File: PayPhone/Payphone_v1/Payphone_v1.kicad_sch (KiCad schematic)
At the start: 70 parts, among them J1 JST_05, J10 PINHD_1x2_Male, J2 Molex_26-60-4030, J3 Molex_26-60-4040, J6 PINHD_1x5_Male, J7 PINHD_1x2_Male, J8 PINHD_1x2_Male, J9 PINHD_1x2_Male, K1 G6S-2, Q2 2N7000, Q3 IRF630, Q4 2N7000, Q5 2N7000, U1 MCP23008-xP, U2 MC34063AP, U3 UC3843AN

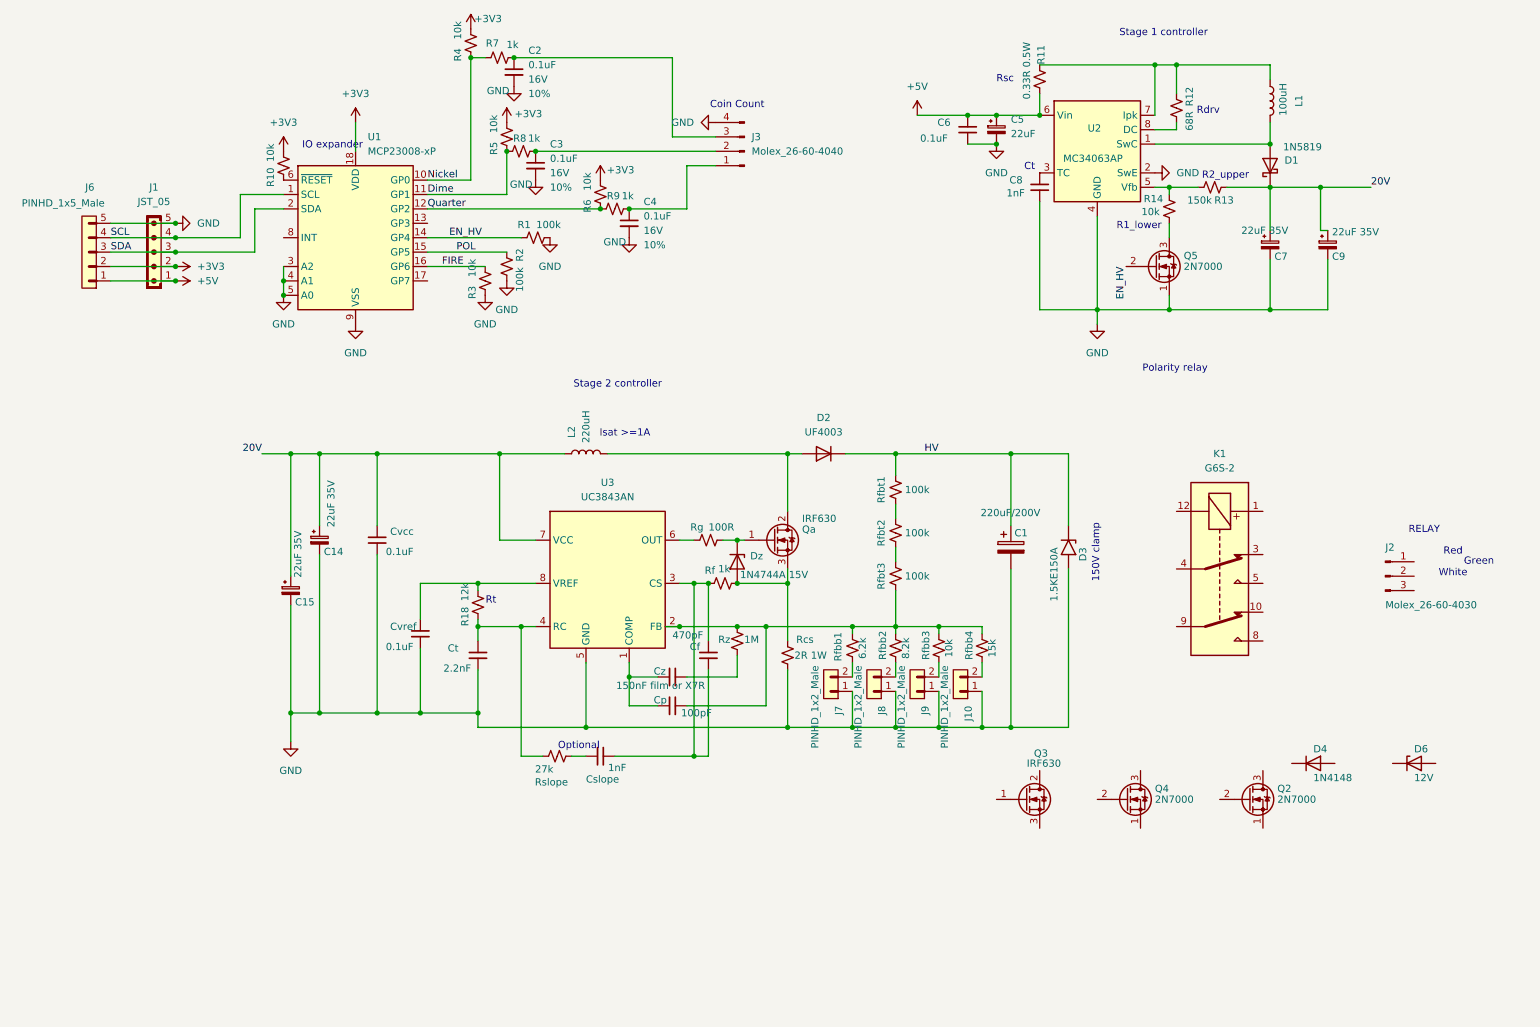
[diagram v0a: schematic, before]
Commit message: Payphone_v1: output stage connected by net labels (K1 contacts, COIL_A/B, RETURN, relay driver, Q4/Q6 gate drive, ISENSE), Q6 2N3906, R20-R26, C16 decoupling for U1; HV-class labels on SW2 and the HV resistor chains
Co-Authored-By: Claude Opus 5.5 <noreply@anthropic.com>
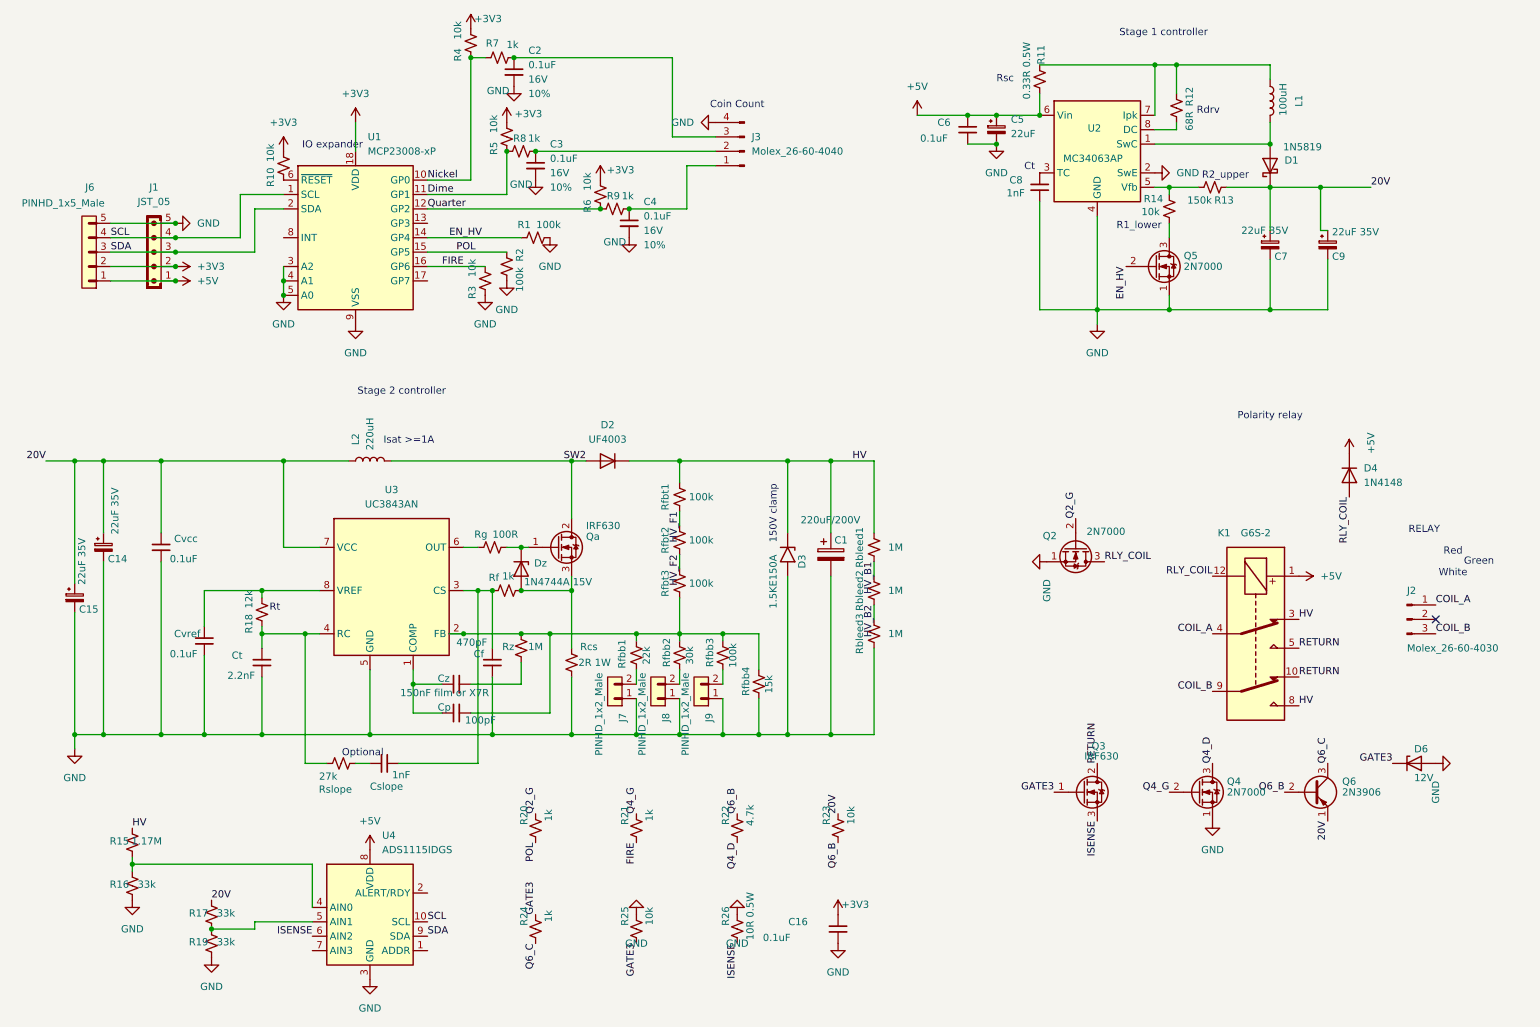
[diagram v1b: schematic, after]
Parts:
- removed J10: PINHD_1x2_Male, Connector_PinHeader_2.54mm:PinHeader_1x02_P2.54mm_Vertical, symbol PCM_SL_Pin_Headers:PINHD_1x2_Male
- added C16: 0.1uF, Capacitor_THT:C_Disc_D5.0mm_W2.5mm_P5.00mm, symbol Device:C_Small
- added Q6: 2N3906, Package_TO_SOT_THT:TO-92_Inline, symbol Transistor_BJT:2N3906
- added R15: 1.17M, Resistor_THT:R_Axial_DIN0207_L6.3mm_D2.5mm_P10.16mm_Horizontal, symbol PCM_SparkFun-Resistor:R_Small
- added R16, R17, R19: 33k, Resistor_THT:R_Axial_DIN0207_L6.3mm_D2.5mm_P10.16mm_Horizontal, symbol PCM_SparkFun-Resistor:R_Small
- added R20, R21, R24: 1k, Resistor_THT:R_Axial_DIN0207_L6.3mm_D2.5mm_P10.16mm_Horizontal, symbol PCM_SparkFun-Resistor:R_Small
- added R22: 4.7k, Resistor_THT:R_Axial_DIN0207_L6.3mm_D2.5mm_P10.16mm_Horizontal, symbol PCM_SparkFun-Resistor:R_Small
- added R23, R25: 10k, Resistor_THT:R_Axial_DIN0207_L6.3mm_D2.5mm_P10.16mm_Horizontal, symbol PCM_SparkFun-Resistor:R_Small
- added R26: 10R 0.5W, Resistor_THT:R_Axial_DIN0309_L9.0mm_D3.2mm_P12.70mm_Horizontal, symbol PCM_SparkFun-Resistor:R_Small
- added Rbleed1, Rbleed2, Rbleed3: 1M, Resistor_THT:R_Axial_DIN0207_L6.3mm_D2.5mm_P10.16mm_Horizontal, symbol PCM_SparkFun-Resistor:R_Small
- added U4: ADS1115IDGS, Package_SO:TSSOP-10_3x3mm_P0.5mm, symbol Analog_ADC:ADS1115IDGS
- Rfbb1: value 6.2k -> 22k
- Rfbb2: value 8.2k -> 30k
- Rfbb3: value 10k -> 100k
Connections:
- net +3V3: now also C16.1
- net +5V: now also D4.1 (K), K1.1, U4.8 (VDD)
- net 20V: now also Q6.1 (E), R17.2, R23.2
- net FIRE: now also R21.1
- net GND: now also Cf.1, D6.2 (A), Q2.1 (S), Q4.1 (S), Rfbb4.1, C16.2, R16.1, R19.1, R25.2, R26.2, Rbleed3.1, U4.3 (GND)
- net HV: now also K1.3, K1.8, R15.2, Rbleed1.2
- net POL: now also R20.1
- net SCL: now also U4.10 (SCL)
- net SDA: now also U4.9 (SDA)
- net at Cf.2, Cslope.1, Rf.2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: no longer Cf.1
- net HV_F2: now reaches Rfbt2.1, Rfbt3.2
- net HV_F1: now reaches Rfbt1.1, Rfbt2.2
- net Q4_G: now reaches Q4.2 (G)
- net Q4_G: now also R21.2
- net Q4_D: now reaches Q4.3 (D)
- net Q4_D: now also R22.1
- net RLY_COIL: now reaches D4.2 (A)
- net RLY_COIL: now also K1.12, Q2.3 (D)
- net GATE3: now reaches D6.1 (K)
- net GATE3: now also Q3.1 (G), R24.2, R25.1
- net SW2: now reaches D2.2 (A), L2.2, Qa.2 (D)
- net RETURN: now reaches K1.10
- net RETURN: now also K1.5, Q3.2 (D)
- net COIL_A: now reaches K1.4
- net COIL_A: now also J2.1 (Pin_1)
- net COIL_B: now reaches K1.9
- net COIL_B: now also J2.3 (Pin_3)
- net ISENSE: now reaches Q3.3 (S)
- net ISENSE: now also R26.1, U4.6 (AIN2)
- net Q2_G: now reaches Q2.2 (G)
- net Q2_G: now also R20.2
- new net: R17.1, R19.2, U4.5 (AIN1)
- new net: R15.1, R16.2, U4.4 (AIN0)
- new net HV_B1: Rbleed1.1, Rbleed2.2
- new net HV_B2: Rbleed2.1, Rbleed3.2
- new net Q6_B: Q6.2 (B), R22.2, R23.1
- new net Q6_C: Q6.3 (C), R24.1
- no-connect marks 0 -> 1
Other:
- moved on the sheet: C1, C14, C15, Cf, Cp, Cslope, Ct, Cvcc, Cvref, Cz, D2, D3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
